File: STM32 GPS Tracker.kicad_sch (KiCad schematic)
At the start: 0 parts

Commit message: Placed MCU STM-32 in Schematic
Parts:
- added U1: STM32F030C8Tx, Package_QFP:LQFP-48_7x7mm_P0.5mm, symbol MCU_ST_STM32F0:STM32F030C8Tx
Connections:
- new net: U1.23 (VSS), U1.47 (VSS)
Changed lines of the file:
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@@
 	(generator_version "9.0")
 	(paper "A4")
+	(symbol
+		(lib_id "MCU_ST_STM32F0:STM32F030C8Tx")
+		(at 243.84 68.58 0)
+		(unit 1)
+		(exclude_from_sim no)
+		(in_bom yes)
+		(on_board yes)
+		(dnp no)
+		(fields_autoplaced yes)
+		(property "Reference" "U1"
+			(at 248.5233 111.76 0)
+			(effects
+				(font
+					(size 1.27 1.27)
+				)
+				(justify left)
+			)
+		)
+		(property "Value" "STM32F030C8Tx"
+			(at 248.5233 114.3 0)
+			(effects
+				(font
+					(size 1.27 1.27)
+				)
+				(justify left)
+			)
+		)
+		(property "Footprint" "Package_QFP:LQFP-48_7x7mm_P0.5mm"
+			(at 231.14 109.22 0)
+			(effects
+				(font
+					(size 1.27 1.27)
+				)
+				(justify right)
+				(hide yes)
+			)
+		)
+		(property "Datasheet" "https://www.st.com/resource/en/datasheet/stm32f030c8.pdf"
+			(at 243.84 68.58 0)
+			(effects
+				(font
+					(size 1.27 1.27)
+				)
+				(hide yes)
+			)
+		)
+		(property "Description" "STMicroelectronics Arm Cortex-M0 MCU, 64KB flash, 8KB RAM, 48 MHz, 2.4-3.6V, 39 GPIO, LQFP48"
+			(at 243.84 68.58 0)
+			(effects
+				(font
+					(size 1.27 1.27)
+				)
+				(hide yes)
+			)
+		)
+		(pin "7"
+		)
+		(pin "2"
+		)
+		(pin "1"
+		)
+		(pin "28"
+		)
+		(pin "47"
+		)
+		(pin "40"
+		)
+		(pin "20"
+		)
+		(pin "6"
+		)
+		(pin "3"
+		)
+		(pin "35"
+		)
+		(pin "41"
+		)
+		(pin "39"
+		)
+		(pin "5"
+		)
+		(pin "43"
+		)
+		(pin "21"
+		)
+		(pin "44"
+		)
+		(pin "36"
+		)
+		(pin "19"
+		)
+		(pin "4"
+		)
+		(pin "18"
+		)
+		(pin "45"
+		)
+		(pin "22"
+		)
+		(pin "25"
+		)
+		(pin "26"
+		)
+		(pin "42"
+		)
+		(pin "46"
+		)
+		(pin "27"
+		)
+		(pin "24"
+		)
+		(pin "23"
+		)
+		(pin "15"
+		)
+		(pin "14"
+		)
+		(pin "10"
+		)
+		(pin "13"
+		)
+		(pin "31"
+		)
+		(pin "29"
+		)
+		(pin "34"
+		)
+		(pin "38"
+		)
+		(pin "9"
+		)
+		(pin "32"
+		)
+		(pin "16"
+		)
+		(pin "30"
+		)
+		(pin "8"
+		)
+		(pin "33"
+		)
+		(pin "48"
+		)
+		(pin "37"
+		)
+		(pin "11"
+		)
+		(pin "12"
+		)
+		(pin "17"
+		)
+		(instances
+			(project ""
+				(path "/320039b8-7fce-4c2b-9942-11f4784b13b1"
+					(reference "U1")
+					(unit 1)
+				)
+			)
+		)
+	)
 	(sheet_instances
 		(path "/"

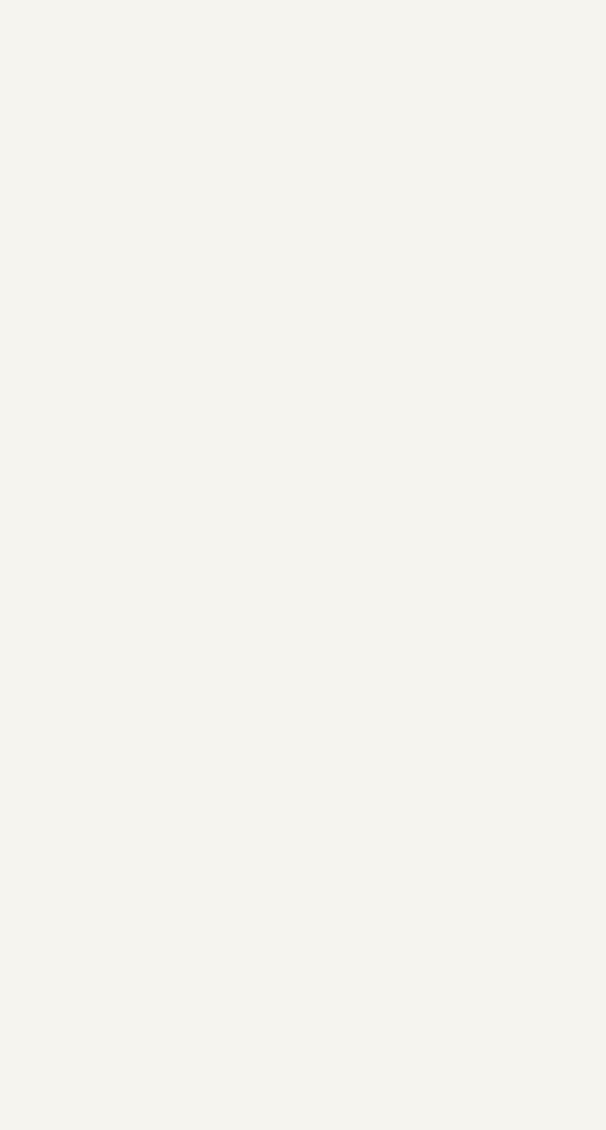
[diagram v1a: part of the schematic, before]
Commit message: Added external Library to Library folder - SIM808
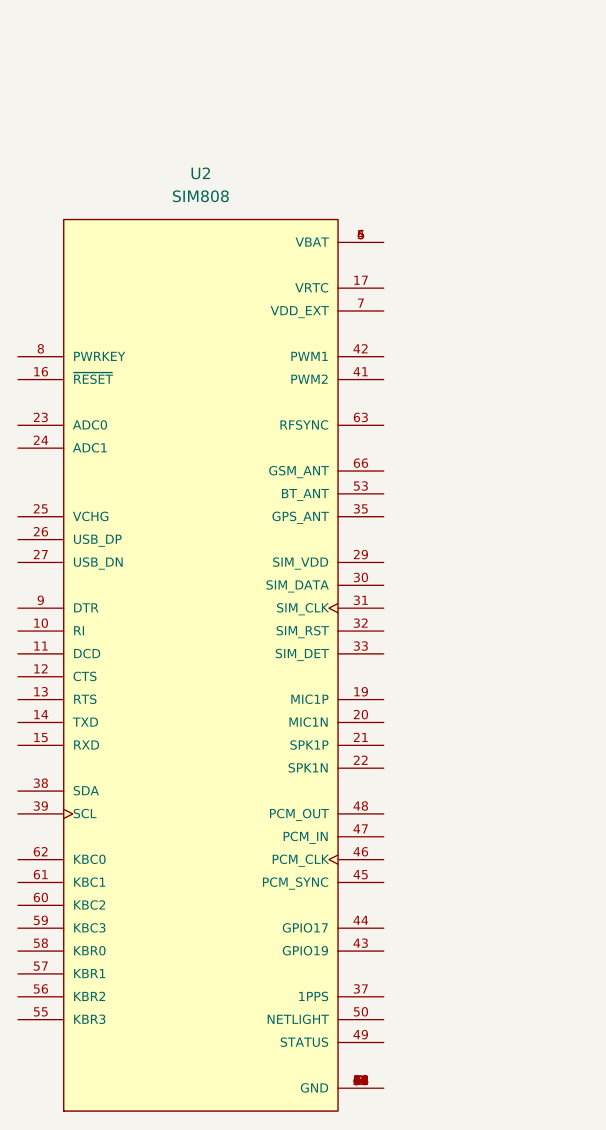
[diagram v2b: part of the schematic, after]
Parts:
- added U2: SIM808, SIM808:XCVR_SIM808, symbol SIM808:SIM808
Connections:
- new net: U2.1 (GND), U2.18 (GND), U2.2 (GND), U2.28 (GND), U2.3 (GND), U2.34 (GND), U2.36 (GND), U2.40 (GND), U2.51 (GND), U2.52 (GND), U2.54 (GND), U2.64 (GND), U2.65 (GND), U2.67 (GND), U2.68 (GND)
- new net: U2.4 (VBAT), U2.5 (VBAT), U2.6 (VBAT)

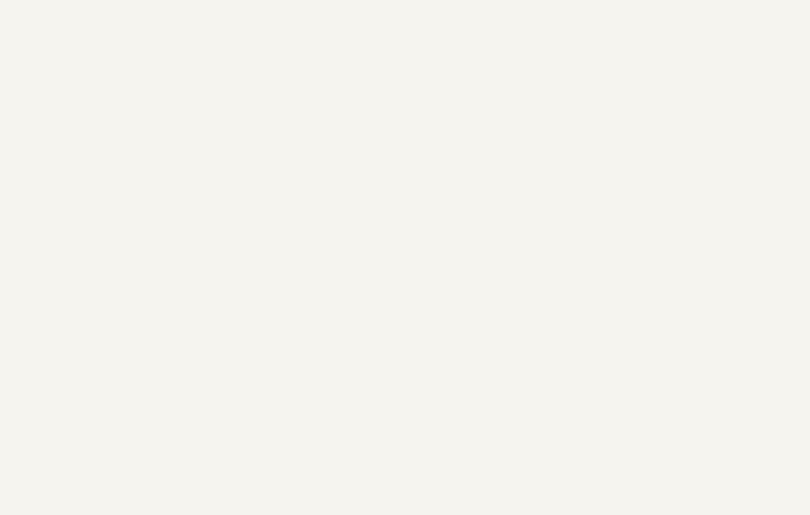
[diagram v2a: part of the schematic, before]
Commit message: Added External Library to Libraries folder - 693010020611 Header for Mini SIM card
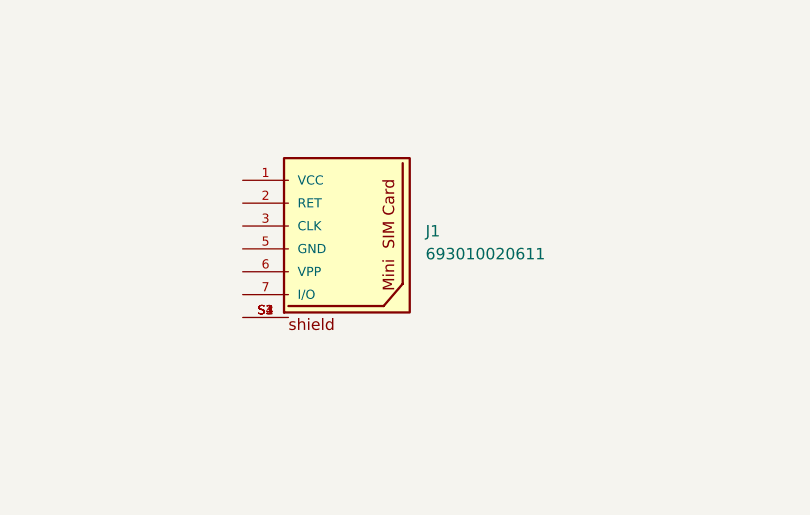
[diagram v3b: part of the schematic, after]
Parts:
- added J1: 693010020611, 693010020611:693010020611, symbol 693010020611:693010020611
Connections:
- new net: J1.S1, J1.S2, J1.S3, J1.S4

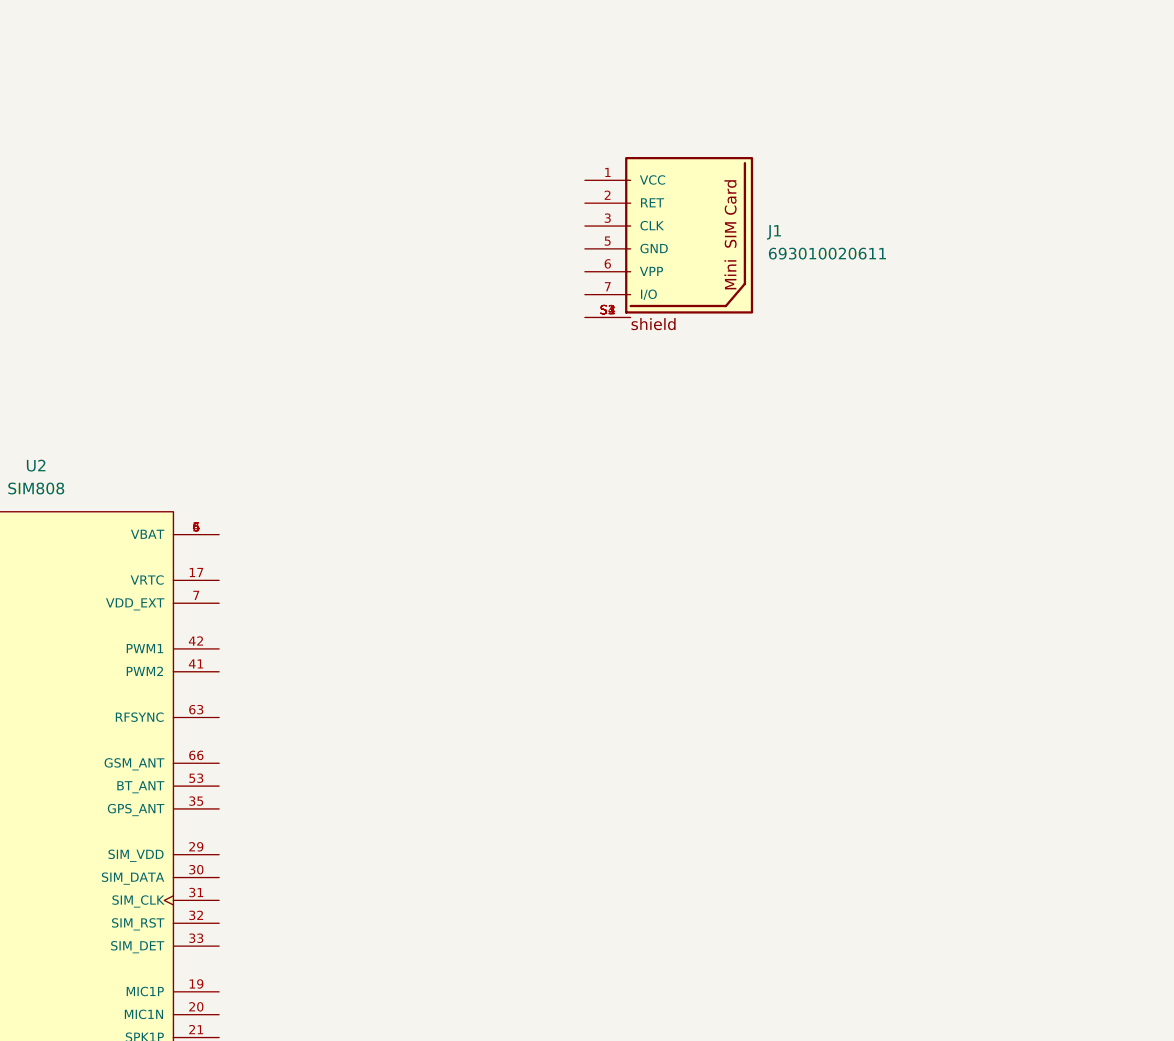
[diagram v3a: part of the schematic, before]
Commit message: Added External Library to Libraries folder - SMF05CT1G
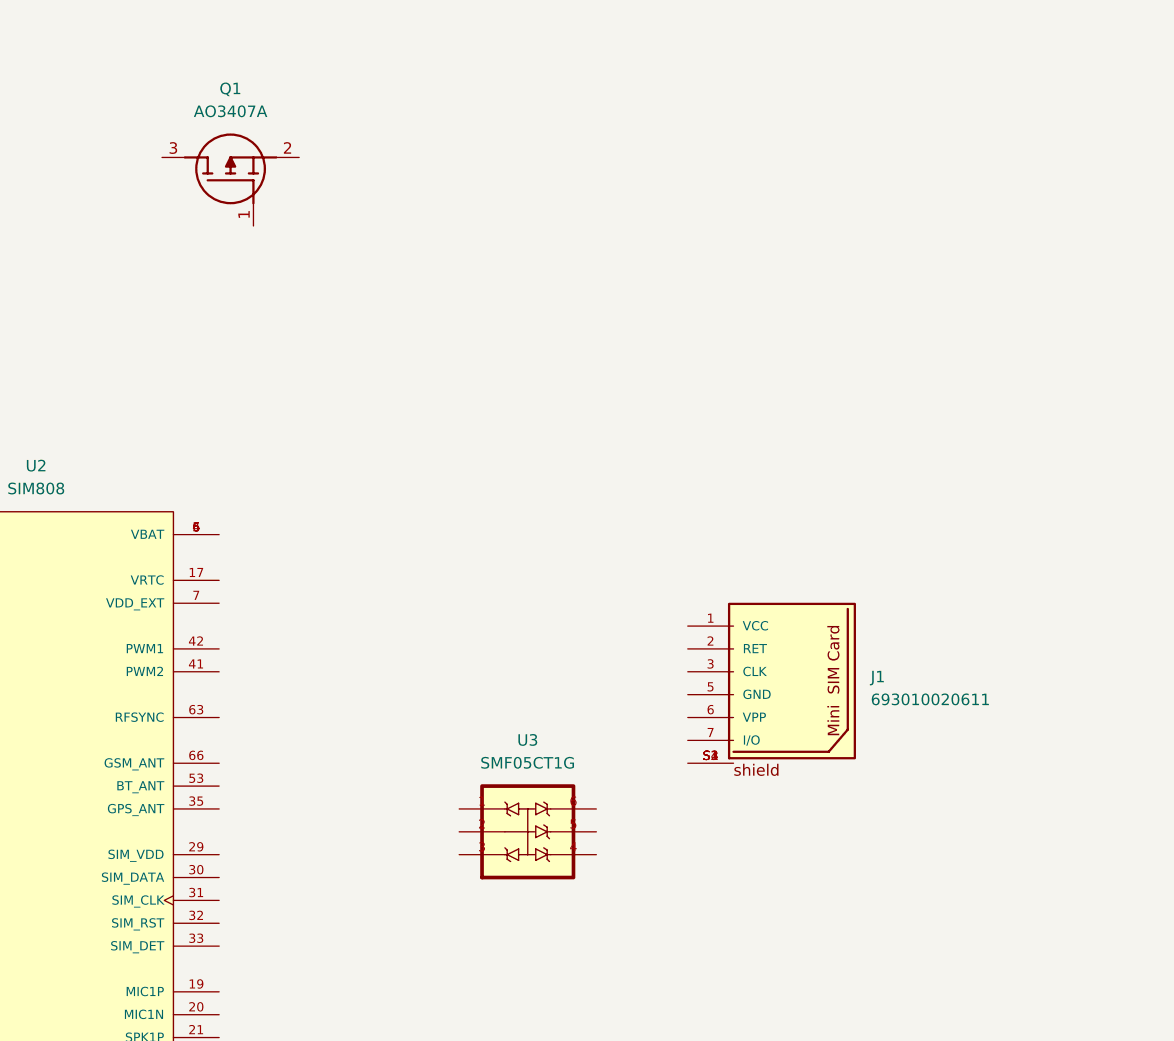
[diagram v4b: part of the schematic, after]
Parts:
- added Q1: AO3407A, SOT95P280X125-3N, symbol AO3407A:AO3407A
- added U3: SMF05CT1G, SMF05CT1G:SOT65P210X110-6N, symbol SMF05CT1G:SMF05CT1G
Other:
- moved on the sheet: J1

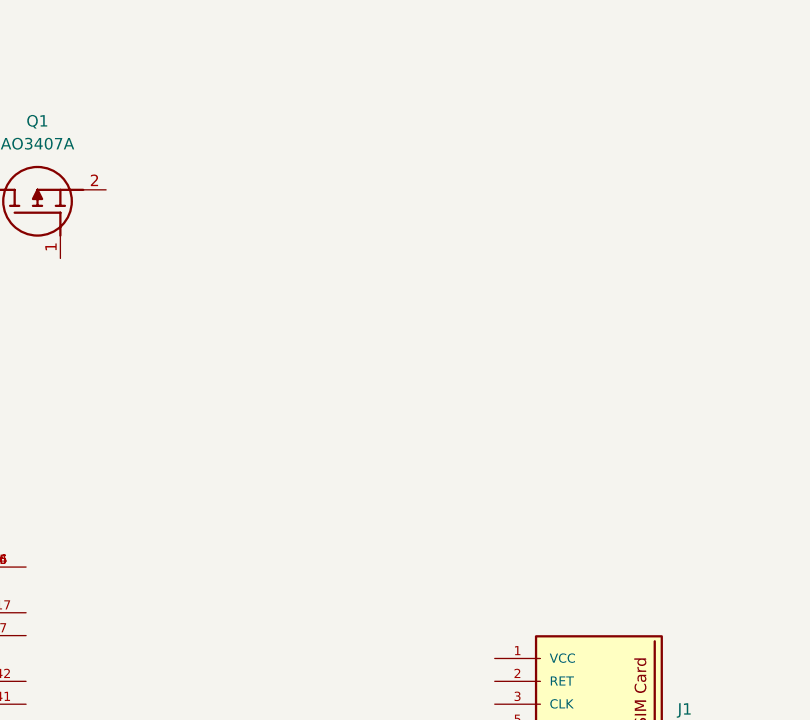
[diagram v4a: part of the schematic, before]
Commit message: Added External Library to Libraries folder - U.FL-R-SMT-1 RF Connector
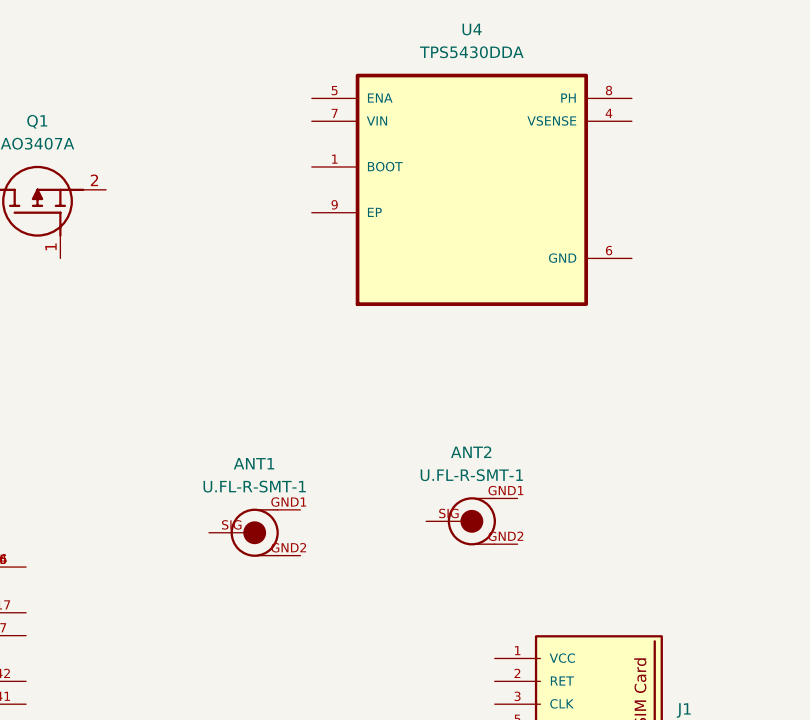
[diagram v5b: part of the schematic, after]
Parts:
- added ANT1, ANT2: U.FL-R-SMT-1, U.FL-R-SMT-1:U.FL-R-SMT-1, symbol U.FL-R-SMT-1:U.FL-R-SMT-1
- added U4: TPS5430DDA, TPS5430DDA:VREG_LM5017MR_NOPB, symbol TPS5430DDA:TPS5430DDA

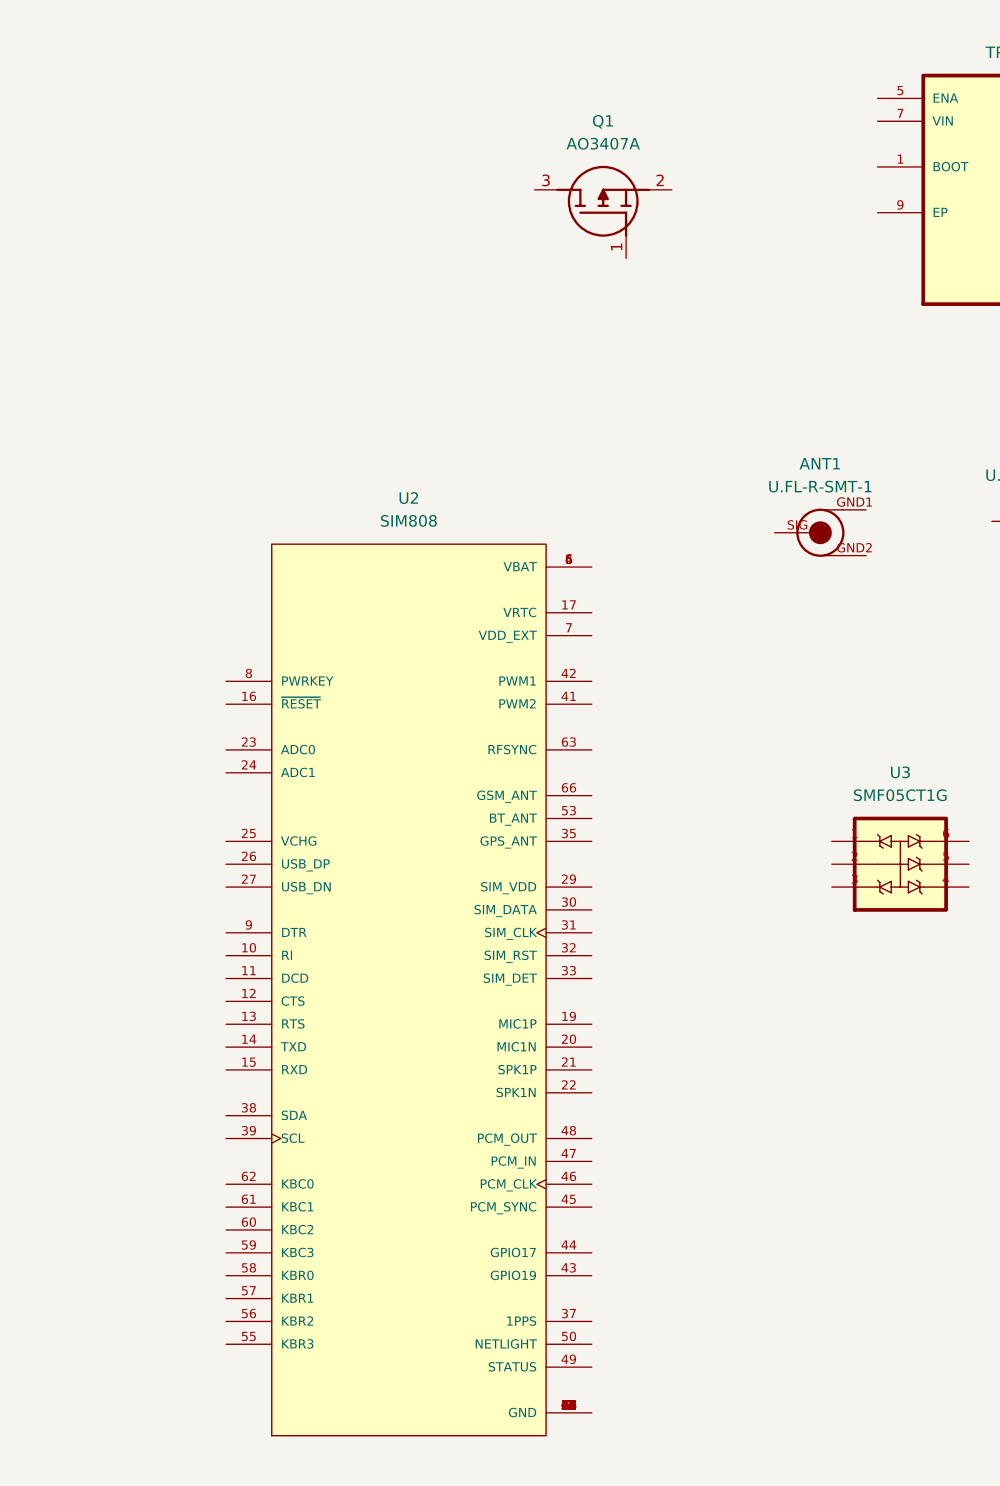
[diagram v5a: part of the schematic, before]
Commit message: Schematic for SIM808 completed
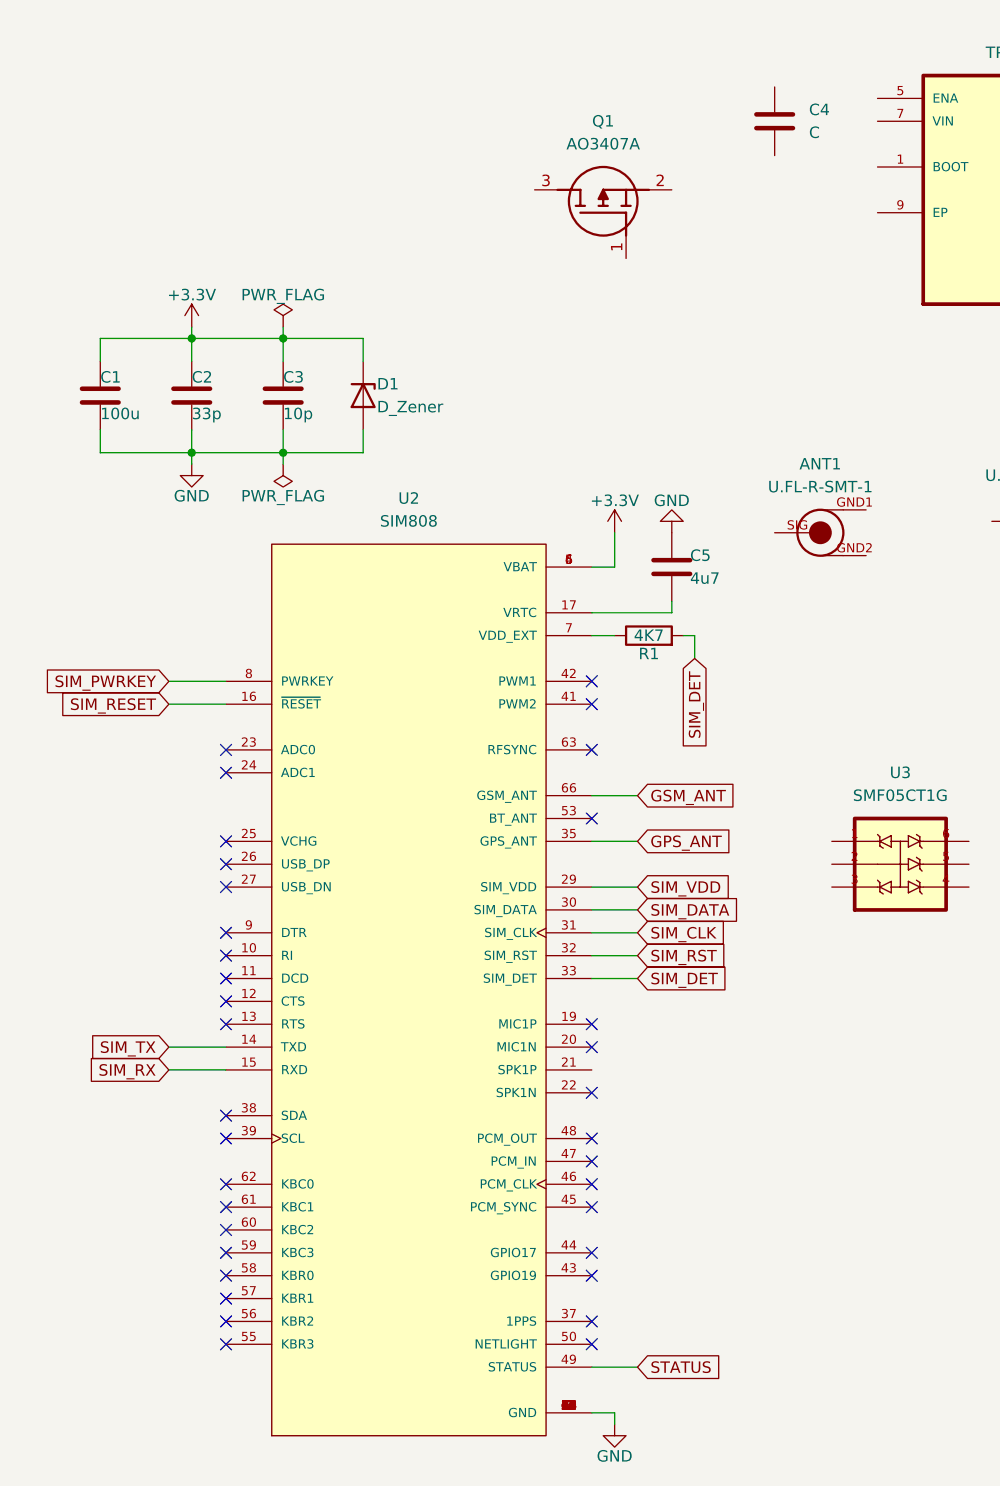
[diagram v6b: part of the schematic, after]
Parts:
- added C1: 100u, symbol Device:C
- added C2: 33p, symbol Device:C
- added C3: 10p, symbol Device:C
- added C4: C, symbol Device:C
- added C5: 4u7, symbol Device:C
- added D1: D_Zener, symbol Device:D_Zener
- added R1: 4K7, symbol Device:R
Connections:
- net GND: now reaches U2.1 (GND), U2.18 (GND), U2.2 (GND), U2.28 (GND), U2.3 (GND), U2.34 (GND), U2.36 (GND), U2.40 (GND), U2.51 (GND), U2.52 (GND), U2.54 (GND), U2.64 (GND), U2.65 (GND), U2.67 (GND), U2.68 (GND)
- net GND: now also C1.2, C2.2, C3.2, C5.1, D1.2 (A)
- net SIM_TX: now reaches U2.14 (TXD)
- net SIM_RX: now reaches U2.15 (RXD)
- net SIM_RESET: now reaches U2.16 (~{RESET})
- net at U2.17 (VRTC): now also C5.2
- net SIM_VDD: now reaches U2.29 (SIM_VDD)
- net SIM_DATA: now reaches U2.30 (SIM_DATA)
- net SIM_CLK: now reaches U2.31 (SIM_CLK)
- net SIM_RST: now reaches U2.32 (SIM_RST)
- net SIM_DET: now reaches U2.33 (SIM_DET)
- net SIM_DET: now also R1.2
- net GPS_ANT: now reaches U2.35 (GPS_ANT)
- net +3.3V: now reaches U2.4 (VBAT), U2.5 (VBAT), U2.6 (VBAT)
- net +3.3V: now also C1.1, C2.1, C3.1, D1.1 (K)
- net STATUS: now reaches U2.49 (STATUS)
- net GSM_ANT: now reaches U2.66 (GSM_ANT)
- net at U2.7 (VDD_EXT): now also R1.1
- net SIM_PWRKEY: now reaches U2.8 (PWRKEY)
- no-connect marks 0 -> 35
